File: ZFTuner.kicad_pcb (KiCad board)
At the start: 4 copper layers, 221.9 x 82 mm, 159 parts, among them J101 RF_In, J102 RF_Out, J103 Tuner, J104 CAN, J201 SWD, J202 USB_C_Receptacle_USB2.0_16P, K401 HF3F-L-12-1ZL2T, K402 HF3F-L-12-1ZL2T, K403 HF3F-L-12-1ZL2T, K404 HF3F-L-12-1ZL2T, K405 HF3F-L-12-1ZL2T, K406 HF3F-L-12-1ZL2T, K407 HF3F-L-12-1ZL2T, K408 HF3F-L-12-1ZL2T, K501 HF3F-L-12-1ZL2T, K502 HF3F-L-12-1ZL2T, K503 HF3F-L-12-1ZL2T, K504 HF3F-L-12-1ZL2T, K505 HF3F-L-12-1ZL2T, K506 HF3F-L-12-1ZL2T, K507 HF3F-L-12-1ZL2T, Q401 PMOS, Q402 PMOS, Q403 NMOS, Q404 NMOS, Q501 PMOS, Q502 PMOS, Q503 NMOS, Q504 NMOS, SW201 CL-SB_22A-12T, U201 ULN2803A, U202 IP4234CZ6, U203 STM32G431CBTx, U204 MCP2542FDxMF, U205 ILD74, U301 LTC5507, U302 LTC5507, U601 HT7463A, U602 BD2243G, U603 MIC5504-3.3YM5, Y201 24MHz

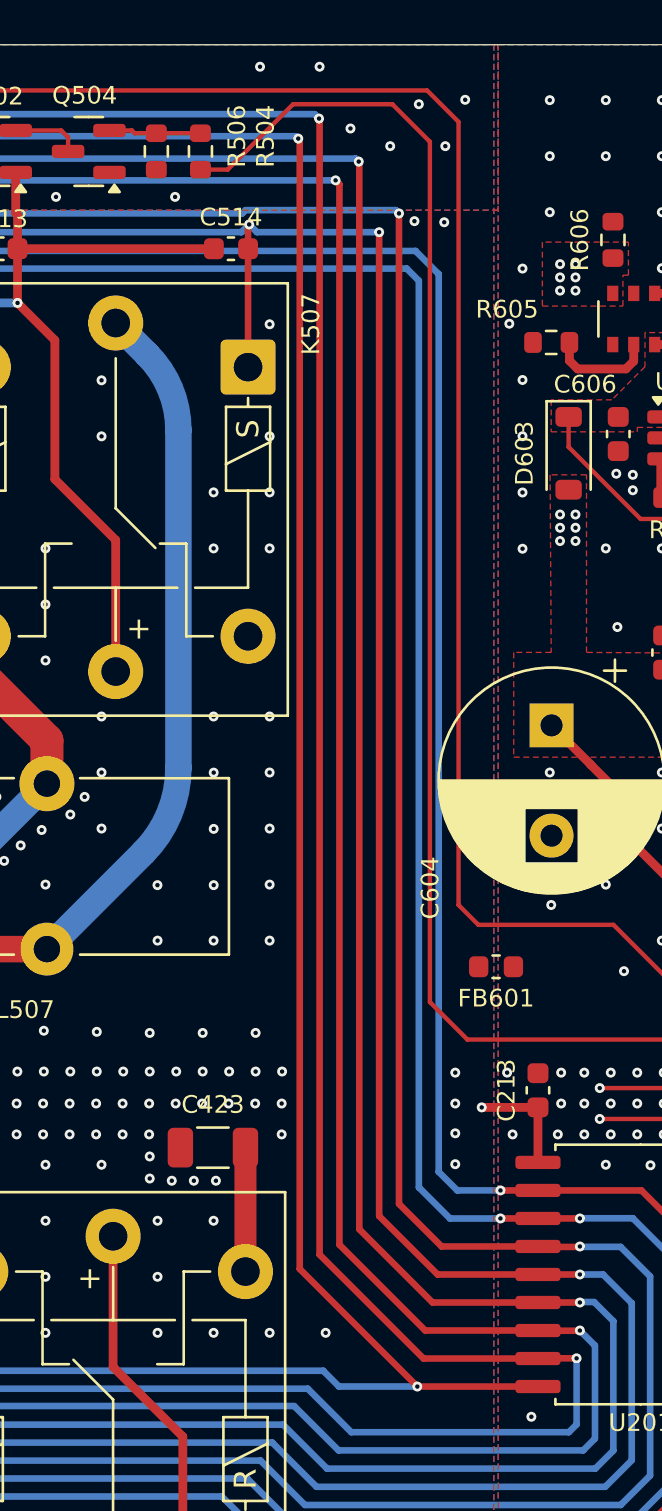
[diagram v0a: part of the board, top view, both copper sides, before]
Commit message: Removed unclear text in schematic. Some minor PCB routing improvments. Added name and revision silkscreen
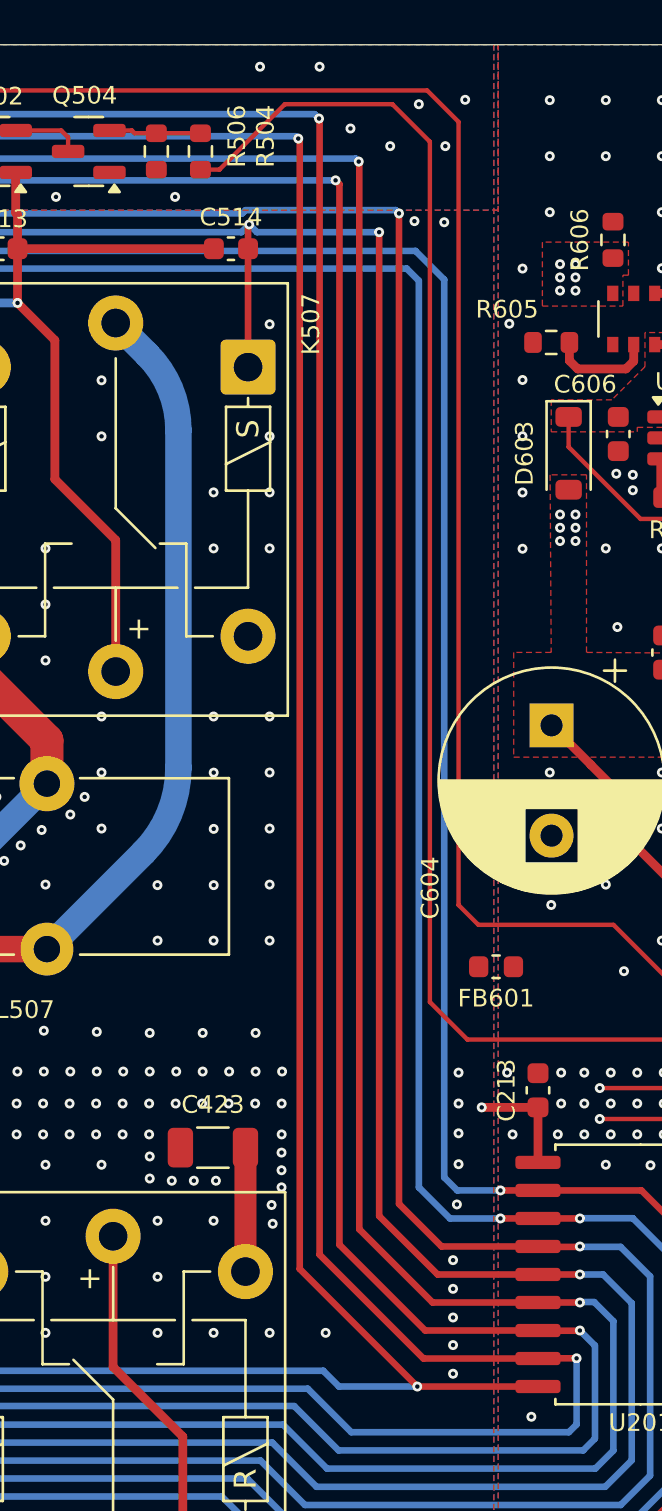
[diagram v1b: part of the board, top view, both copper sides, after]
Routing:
- net GND: vias 1509 -> 1520

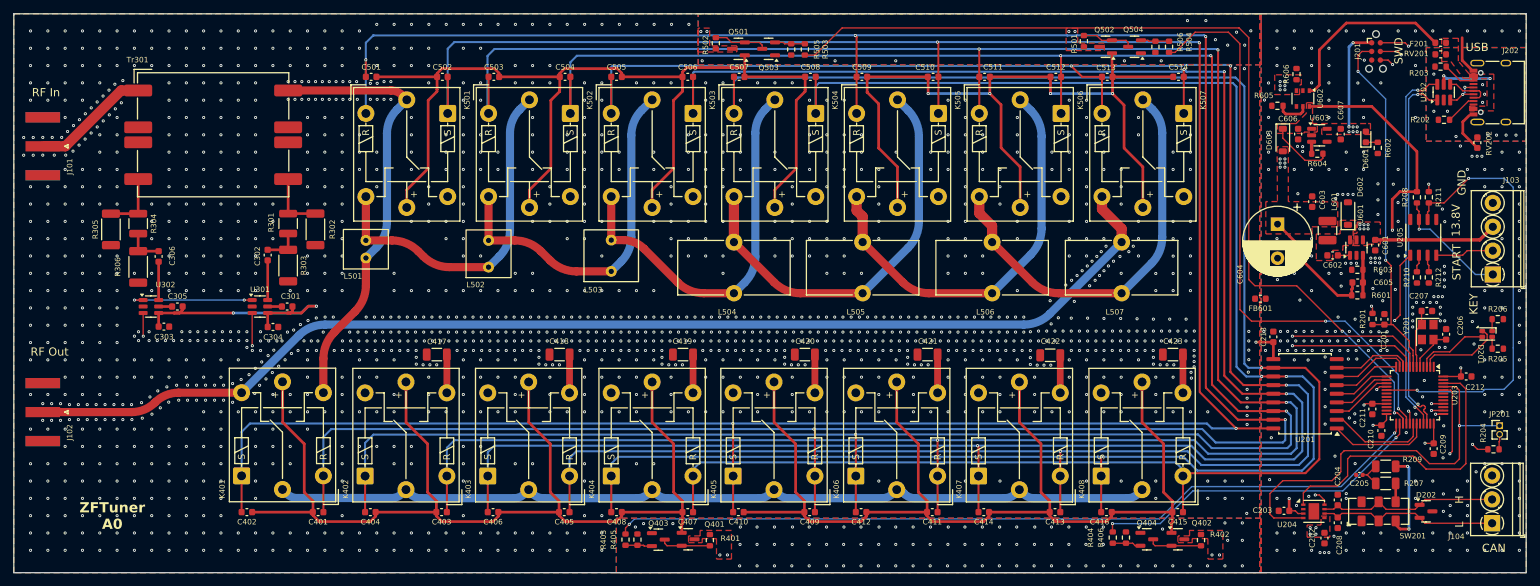
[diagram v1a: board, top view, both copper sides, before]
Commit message: Replaced SMA footprints with correct connectors
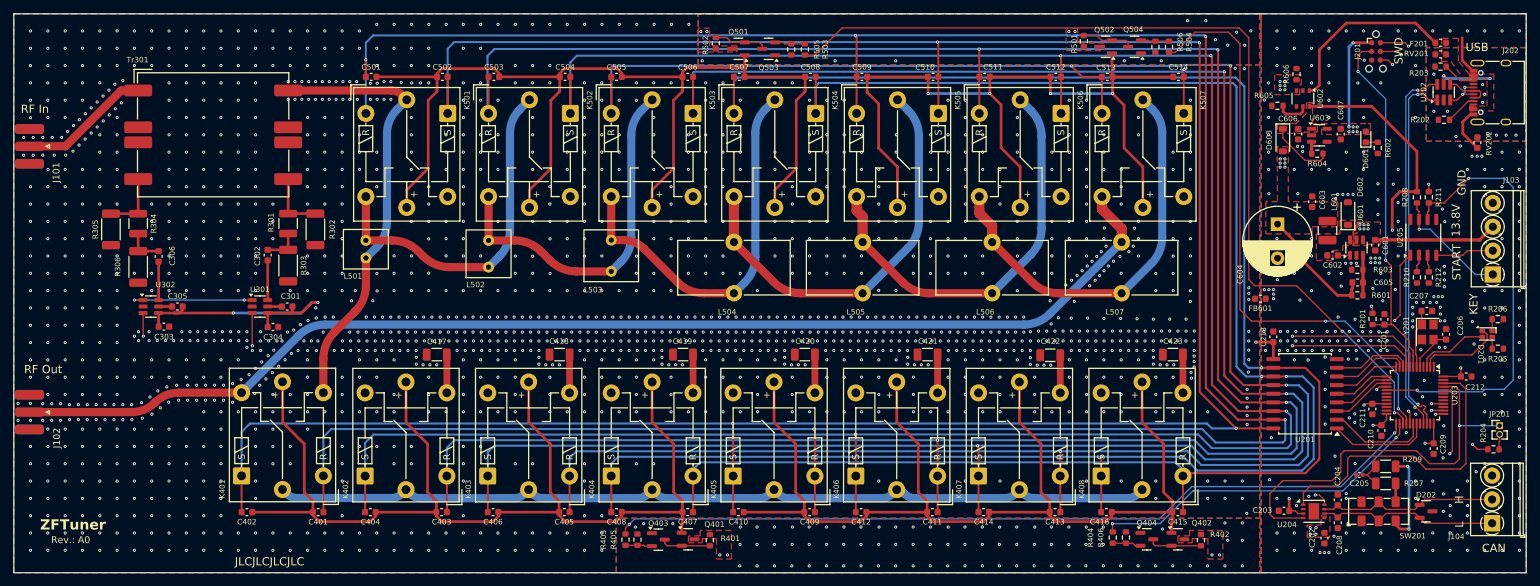
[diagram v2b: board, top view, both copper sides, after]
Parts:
- J101, J102: footprint Connector_Coaxial:SMA_Amphenol_132289_EdgeMount -> Connector_Coaxial:SMA_Bat_Wireless_BWSMA-KE-P001_EdgeMount_1.6mm-PCB
- R601: value 91k -> 95.3k
- R603: value 15.8k -> 16.5k
- moved J101 1.95 mm to (46.3, 60.0), turned to 0 degrees
- moved J102 1.95 mm to (46.3, 98.9), turned to 0 degrees
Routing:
- net /RF_In: track 17.4 -> 19.3 mm
- net /RF_Out: track 175.5 -> 177.5 mm
- net +3.3V: track 242.1 -> 243.0 mm
- net GNDD: vias 370 -> 376
- net GND: vias 1520 -> 1594
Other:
- board text added: "JLCJLCJLCJLC"
- board text added: "Rev.: ${REVISION}"
- board text added: "ZFTuner"
- board text removed: "ZFTuner ${REVISION}"

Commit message: Improved grounding
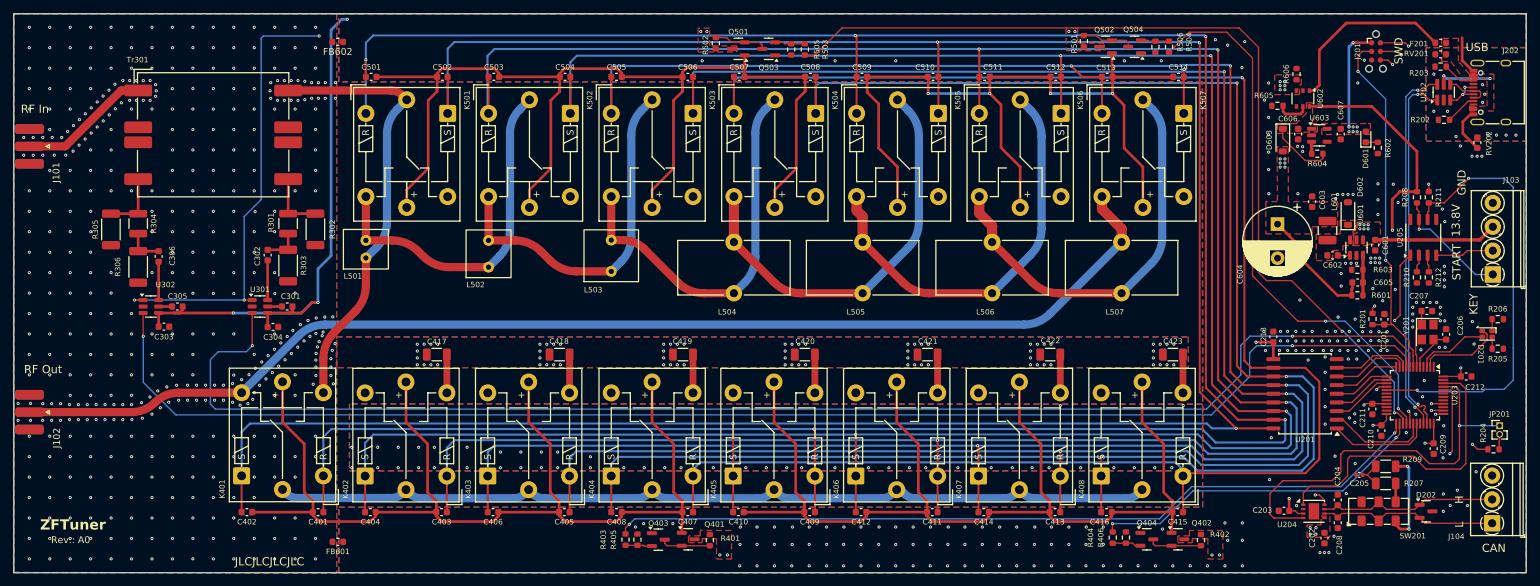
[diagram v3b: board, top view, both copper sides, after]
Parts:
- added FB602: MPZ1608S300A, Inductor_SMD:L_0603_1608Metric, F.Cu at (91.5, 44.6)
- moved FB601 140.0 mm to (91.5, 118.0)
- moved C422 0.10 mm to (196.1, 90.5)
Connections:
- U203 pad 8: /Controller/Fwd_V -> /Controller/Rfl_V
- U203 pad 9: /Controller/Rfl_V -> /Controller/Fwd_V
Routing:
- net /Controller/~{SWR_SHDN}: track 205.5 -> 275.2 mm, vias 3 -> 4
- net +3.3V: track 243.0 -> 282.6 mm, vias 23 -> 21
- net /Controller/Rfl_V: track 176.2 -> 204.6 mm
- net /Controller/Fwd_V: track 192.3 -> 205.8 mm
- net /Controller/IndRels_2: track 86.2 -> 82.1 mm
- net /Controller/IndRels_1: track 137.3 -> 135.9 mm
- net GNDD: vias 376 -> 292
- net GND: vias 1594 -> 525
- removed copper zone on In1.Cu, net +3.3V

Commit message: Improve RF routing
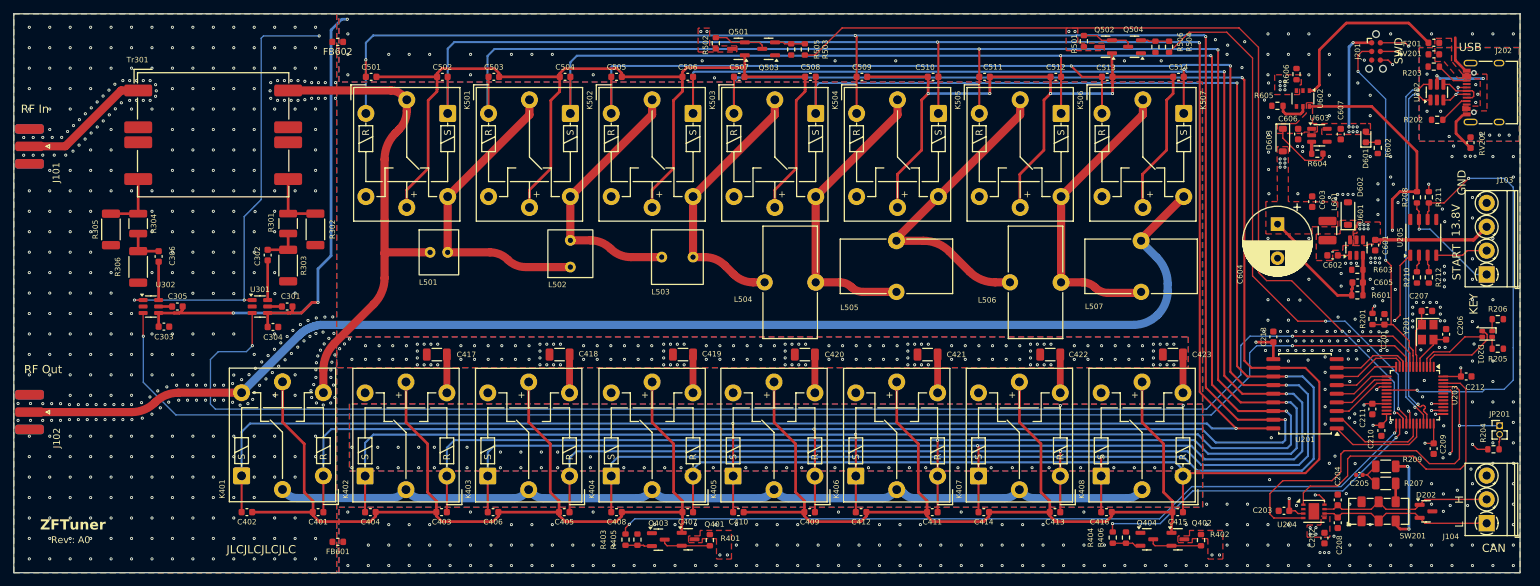
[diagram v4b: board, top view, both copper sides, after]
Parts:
- moved L502 12.0 mm to (125.7, 75.7)
- moved L501 10.7 mm to (106.4, 75.5), turned to 0 degrees
- moved L503 9.71 mm to (141.4, 76.2), turned to 0 degrees
- moved L504 8.53 mm to (157.9, 79.9), turned to -90 degrees
- moved L506 6.72 mm to (193.9, 79.9), turned to -90 degrees
- moved L505 4.96 mm to (173.5, 77.5)
- moved L507 2.87 mm to (209.4, 77.5)
- moved F201 1.00 mm to (252.3, 44.8)
- moved J202 1.00 mm to (260.8, 52.1)
- moved R202 1.00 mm to (252.8, 56.1)
- moved R203 1.00 mm to (252.3, 48.2)
- moved RV201 1.00 mm to (252.3, 46.5)
- moved RV202 1.00 mm to (257.7, 59.4)
- moved U202 1.00 mm to (252.8, 52.0)
- moved J103 0.90 mm to (260.1, 78.8)
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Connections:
- K501 pad 12: unconnected-(K501-Pad12) -> /Inductors_Bank/Ind1
- K501 pad 14: /Inductors_Bank/Ind1 -> unconnected-(K501-Pad14)
- K502 pad 12: unconnected-(K502-Pad12) -> /Inductors_Bank/Ind2
- K502 pad 14: /Inductors_Bank/Ind2 -> unconnected-(K502-Pad14)
- K503 pad 12: unconnected-(K503-Pad12) -> /Inductors_Bank/Ind3
- K503 pad 14: /Inductors_Bank/Ind3 -> unconnected-(K503-Pad14)
- K504 pad 12: unconnected-(K504-Pad12) -> /Inductors_Bank/Ind4
- K504 pad 14: /Inductors_Bank/Ind4 -> unconnected-(K504-Pad14)
- K505 pad 12: unconnected-(K505-Pad12) -> /Inductors_Bank/Ind5
- K505 pad 14: /Inductors_Bank/Ind5 -> unconnected-(K505-Pad14)
- K506 pad 12: unconnected-(K506-Pad12) -> /Inductors_Bank/Ind6
- K506 pad 14: /Inductors_Bank/Ind6 -> unconnected-(K506-Pad14)
- K507 pad 12: unconnected-(K507-Pad12) -> /RF_Out
- K507 pad 14: /RF_Out -> unconnected-(K507-Pad14)
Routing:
- net /Inductors_Bank/Ind3: track 57.5 -> 39.7 mm
- net /Inductors_Bank/Ind4: track 61.0 -> 43.9 mm
- net /Inductors_Bank/Ind6: track 60.8 -> 43.9 mm
- net /RF_Out: track 177.5 -> 192.3 mm
- net /Inductors_Bank/Ind5: track 61.1 -> 46.9 mm
- net /Inductors_Bank/Ind2: track 53.0 -> 39.6 mm
- net /Capacitors_Bank/RF_In: track 64.9 -> 71.7 mm
- net /Inductors_Bank/Ind1: track 52.1 -> 46.5 mm
- net /Controller/USB_DP: track 54.5 -> 53.4 mm
- net /Controller/USB_DN: track 54.6 -> 53.5 mm
- net VBUS: track 26.8 -> 25.8 mm
- net /CAN_H: track 26.7 -> 25.8 mm
- net /CAN_L: track 26.7 -> 25.8 mm
- net /TUNER_KEY: track 17.5 -> 16.6 mm
- net /TUNER_START: track 8.57 -> 7.67 mm
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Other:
- board size 221.9 x 82 mm -> 221 x 82 mm

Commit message: Readded some vias and fixed board dimensions
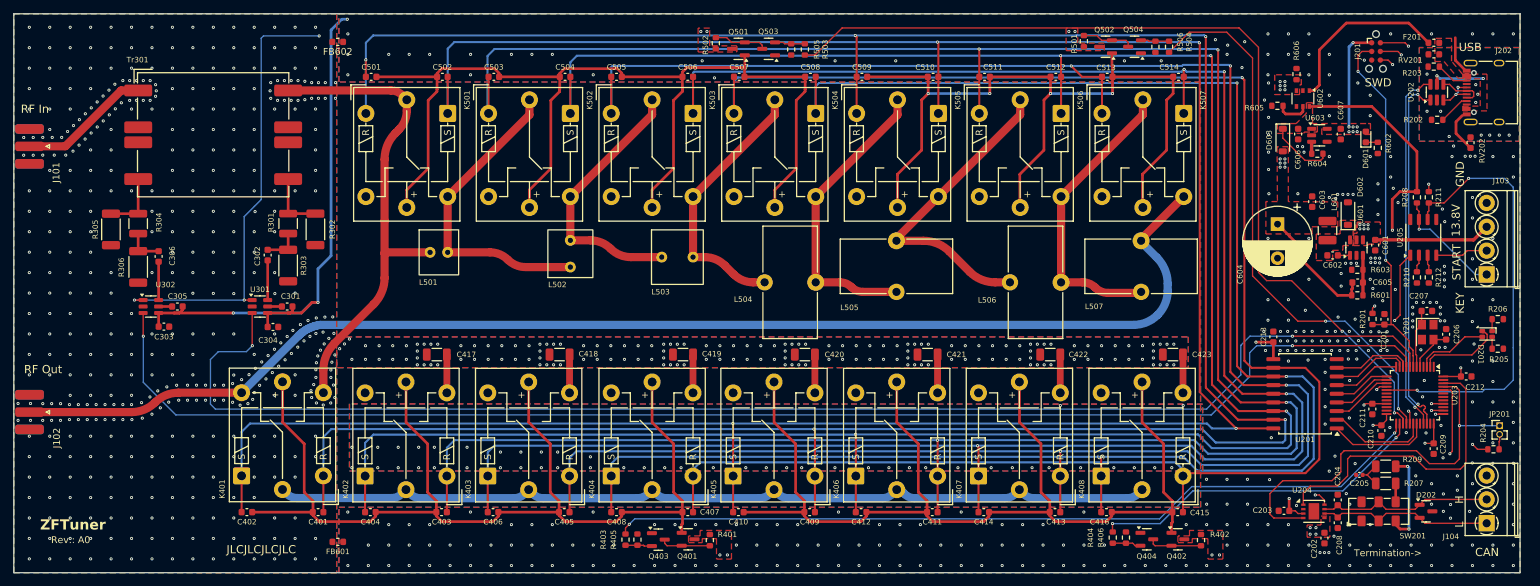
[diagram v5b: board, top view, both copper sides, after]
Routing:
- net GNDD: vias 431 -> 436
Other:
- board text added: "Termination->"
